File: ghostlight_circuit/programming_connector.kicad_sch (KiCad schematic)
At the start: 1 part, among them J1 Conn_01x08

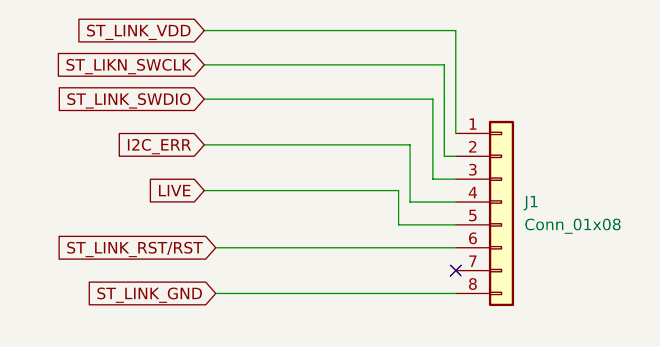
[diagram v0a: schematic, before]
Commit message: update pcb
rerout and connect accelerometer

better re-route
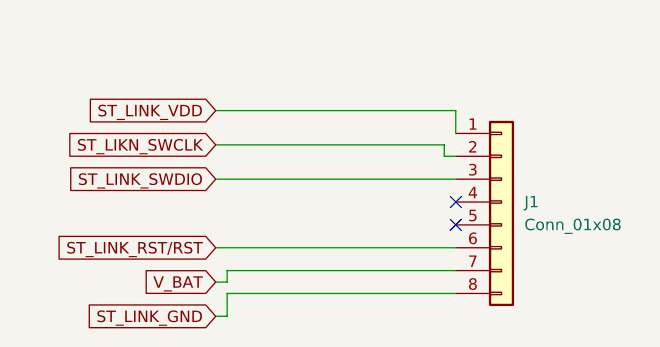
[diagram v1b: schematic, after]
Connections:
- net V_BAT: now reaches J1.7 (Pin_7)
- net I2C_ERR: no longer names the net of J1.4 (Pin_4)
- net LIVE: no longer names the net of J1.5 (Pin_5)
- no-connect marks 1 -> 2
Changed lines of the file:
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@@
 	(paper "A4")
 	(no_connect
-		(at 107.95 100.33)
-	)
-	(wire
-		(pts
-			(xy 80.01 77.47) (xy 106.68 77.47)
-		)
-		(stroke
-			(width 0)
-			(type default)
-		)
-	)
-	(wire
-		(pts
-			(xy 80.01 91.44) (xy 101.6 91.44)
-		)
-		(stroke
-			(width 0)
-			(type default)
-		)
-	)
-	(wire
-		(pts
-			(xy 81.28 102.87) (xy 107.95 102.87)
-		)
-		(stroke
-			(width 0)
-			(type default)
-		)
-	)
-	(wire
-		(pts
-			(xy 105.41 81.28) (xy 105.41 90.17)
-		)
-		(stroke
-			(width 0)
-			(type default)
-		)
-	)
-	(wire
-		(pts
-			(xy 102.87 86.36) (xy 102.87 92.71)
-		)
-		(stroke
-			(width 0)
-			(type default)
-		)
-	)
-	(wire
-		(pts
-			(xy 80.01 86.36) (xy 102.87 86.36)
+		(at 107.95 95.25)
+	)
+	(no_connect
+		(at 107.95 92.71)
+	)
+	(wire
+		(pts
+			(xy 81.28 86.36) (xy 106.68 86.36)
+		)
+		(stroke
+			(width 0)
+			(type default)
+		)
+	)
+	(wire
+		(pts
+			(xy 81.28 105.41) (xy 82.55 105.41)
+		)
+		(stroke
+			(width 0)
+			(type default)
+		)
+	)
+	(wire
+		(pts
+			(xy 82.55 102.87) (xy 107.95 102.87)
 		)
 		(stroke
@@
 	(wire
 		(pts
-			(xy 101.6 95.25) (xy 107.95 95.25)
-		)
-		(stroke
-			(width 0)
-			(type default)
-		)
-	)
-	(wire
-		(pts
-			(xy 101.6 91.44) (xy 101.6 95.25)
-		)
-		(stroke
-			(width 0)
-			(type default)
-		)
-	)
-	(wire
-		(pts
-			(xy 80.01 81.28) (xy 105.41 81.28)
-		)
-		(stroke
-			(width 0)
-			(type default)
-		)
-	)
-	(wire
-		(pts
-			(xy 107.95 73.66) (xy 107.95 85.09)
-		)
-		(stroke
-			(width 0)
-			(type default)
-		)
-	)
-	(wire
-		(pts
-			(xy 102.87 92.71) (xy 107.95 92.71)
-		)
-		(stroke
-			(width 0)
-			(type default)
-		)
-	)
-	(wire
-		(pts
-			(xy 105.41 90.17) (xy 107.95 90.17)
-		)
-		(stroke
-			(width 0)
-			(type default)
-		)
-	)
-	(wire
-		(pts
-			(xy 80.01 73.66) (xy 107.95 73.66)
+			(xy 82.55 101.6) (xy 82.55 100.33)
+		)
+		(stroke
+			(width 0)
+			(type default)
+		)
+	)
+	(wire
+		(pts
+			(xy 82.55 100.33) (xy 107.95 100.33)
+		)
+		(stroke
+			(width 0)
+			(type default)
+		)
+	)
+	(wire
+		(pts
+			(xy 81.28 90.17) (xy 107.95 90.17)
+		)
+		(stroke
+			(width 0)
+			(type default)
+		)
+	)
+	(wire
+		(pts
+			(xy 107.95 82.55) (xy 107.95 85.09)
+		)
+		(stroke
+			(width 0)
+			(type default)
+		)
+	)
+	(wire
+		(pts
+			(xy 81.28 82.55) (xy 107.95 82.55)
+		)
+		(stroke
+			(width 0)
+			(type default)
+		)
+	)
+	(wire
+		(pts
+			(xy 82.55 105.41) (xy 82.55 102.87)
 		)
 		(stroke
@@
 	(wire
 		(pts
-			(xy 106.68 77.47) (xy 106.68 87.63)
+			(xy 81.28 101.6) (xy 82.55 101.6)
+		)
+		(stroke
+			(width 0)
+			(type default)
+		)
+	)
+	(wire
+		(pts
+			(xy 106.68 86.36) (xy 106.68 87.63)
 		)
 		(stroke
@@
 	(global_label "ST_LINK_VDD"
 		(shape input)
-		(at 80.01 73.66 180)
-		(fields_autoplaced yes)
-		(effects
-			(font
-				(size 1.27 1.27)
-			)
-			(justify right)
-		)
-		(property "Intersheetrefs" "${INTERSHEET_REFS}"
-			(at 65.0505 73.66 0)
+		(at 81.28 82.55 180)
+		(fields_autoplaced yes)
+		(effects
+			(font
+				(size 1.27 1.27)
+			)
+			(justify right)
+		)
+		(property "Intersheetrefs" "${INTERSHEET_REFS}"
+			(at 66.3205 82.55 0)
 			(hide yes)
 			(show_name no)
@@
 	(global_label "ST_LINK_GND"
 		(shape input)
-		(at 81.28 102.87 180)
-		(fields_autoplaced yes)
-		(effects
-			(font
-				(size 1.27 1.27)
-			)
-			(justify right)
-		)
-		(property "Intersheetrefs" "${INTERSHEET_REFS}"
-			(at 66.0786 102.87 0)
+		(at 81.28 105.41 180)
+		(fields_autoplaced yes)
+		(effects
+			(font
+				(size 1.27 1.27)
+			)
+			(justify right)
+		)
+		(property "Intersheetrefs" "${INTERSHEET_REFS}"
+			(at 66.0786 105.41 0)
 			(hide yes)
 			(show_name no)
@@
 	(global_label "ST_LIKN_SWCLK"
 		(shape input)
-		(at 80.01 77.47 180)
-		(fields_autoplaced yes)
-		(effects
-			(font
-				(size 1.27 1.27)
-			)
-			(justify right)
-		)
-		(property "Intersheetrefs" "${INTERSHEET_REFS}"
-			(at 62.4501 77.47 0)
-			(hide yes)
-			(show_name no)
-			(do_not_autoplace no)
-			(effects
-				(font
-					(size 1.27 1.27)
-				)
-				(justify right)
-			)
-		)
-	)
-	(global_label "I2C_ERR"
-		(shape input)
-		(at 80.01 86.36 180)
-		(fields_autoplaced yes)
-		(effects
-			(font
-				(size 1.27 1.27)
-			)
-			(justify right)
-		)
-		(property "Intersheetrefs" "${INTERSHEET_REFS}"
-			(at 69.2839 86.36 0)
+		(at 81.28 86.36 180)
+		(fields_autoplaced yes)
+		(effects
+			(font
+				(size 1.27 1.27)
+			)
+			(justify right)
+		)
+		(property "Intersheetrefs" "${INTERSHEET_REFS}"
+			(at 63.7201 86.36 0)
 			(hide yes)
 			(show_name no)
@@
 	(global_label "ST_LINK_SWDIO"
 		(shape input)
-		(at 80.01 81.28 180)
-		(fields_autoplaced yes)
-		(effects
-			(font
-				(size 1.27 1.27)
-			)
-			(justify right)
-		)
-		(property "Intersheetrefs" "${INTERSHEET_REFS}"
-			(at 62.8129 81.28 0)
-			(hide yes)
-			(show_name no)
-			(do_not_autoplace no)
-			(effects
-				(font
-					(size 1.27 1.27)
-				)
-				(justify right)
-			)
-		)
-	)
-	(global_label "LIVE"
-		(shape input)
-		(at 80.01 91.44 180)
-		(effects
-			(font
-				(size 1.27 1.27)
-			)
-			(justify right)
-		)
-		(property "Intersheetrefs" "${INTERSHEET_REFS}"
-			(at 80.01 91.44 0)
-			(hide yes)
-			(show_name no)
-			(do_not_autoplace no)
-			(effects
-				(font
-					(size 1.27 1.27)
-				)
-			)
-		)
+		(at 81.28 90.17 180)
+		(fields_autoplaced yes)
+		(effects
+			(font
+				(size 1.27 1.27)
+			)
+			(justify right)
+		)
+		(property "Intersheetrefs" "${INTERSHEET_REFS}"
+			(at 64.0829 90.17 0)
+			(hide yes)
+			(show_name no)
+			(do_not_autoplace no)
+			(effects
+				(font
+					(size 1.27 1.27)
+				)
+				(justify right)
+			)
+		)
+	)
+	(global_label "V_BAT"
+		(shape input)
+		(at 81.28 101.6 180)
+		(fields_autoplaced yes)
+		(effects
+			(font
+				(size 1.27 1.27)
+			)
+			(justify right)
+		)
+		(property "Intersheetrefs" "${INTERSHEET_REFS}"
+			(at 72.9124 101.6 0)
+			(hide yes)
+			(show_name no)
+			(do_not_autoplace no)
+			(effects
+				(font
+					(size 1.27 1.27)
+				)
+				(justify right)
+			)
+		)
